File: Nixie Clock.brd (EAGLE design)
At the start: 226.4 x 128.3 mm, 136 parts, among them IC1_SECONDS_UNITS 4017N, IC2_SECONDS_TENS 4017N, IC3_MINUTES_UNITS 4017N, IC4_MINUTES_TENS 4017N, IC5_HOURS_UNITS 4017N, IC6_HOURS_TENS 4017N, T0 MPSA42, T1 MPSA42, T10 MPSA42, T11 MPSA42, T12 MPSA42, T13 MPSA42, T14 MPSA42, T15 MPSA42, T16 MPSA42, T17 MPSA42, T18 MPSA42, T19 MPSA42, T2 MPSA42, T20 MPSA42, T21 MPSA42, T22 MPSA42, T23 MPSA42, T24 MPSA42, T25 MPSA42, T26 MPSA42, T27 MPSA42, T28 MPSA42, T29 MPSA42, T3 MPSA42, T30 MPSA42, T31 MPSA42, T32 MPSA42, T33 MPSA42, T34 MPSA42, T35 MPSA42, T36 MPSA42, T37 MPSA42, T38 MPSA42, T39 MPSA42, T4 MPSA42, T40 MPSA42, T41 MPSA42, T42 MPSA42, T43 MPSA42, T44 MPSA42, T5 MPSA42, T6 MPSA42, T7 MPSA42, T8 MPSA42, T9 MPSA42

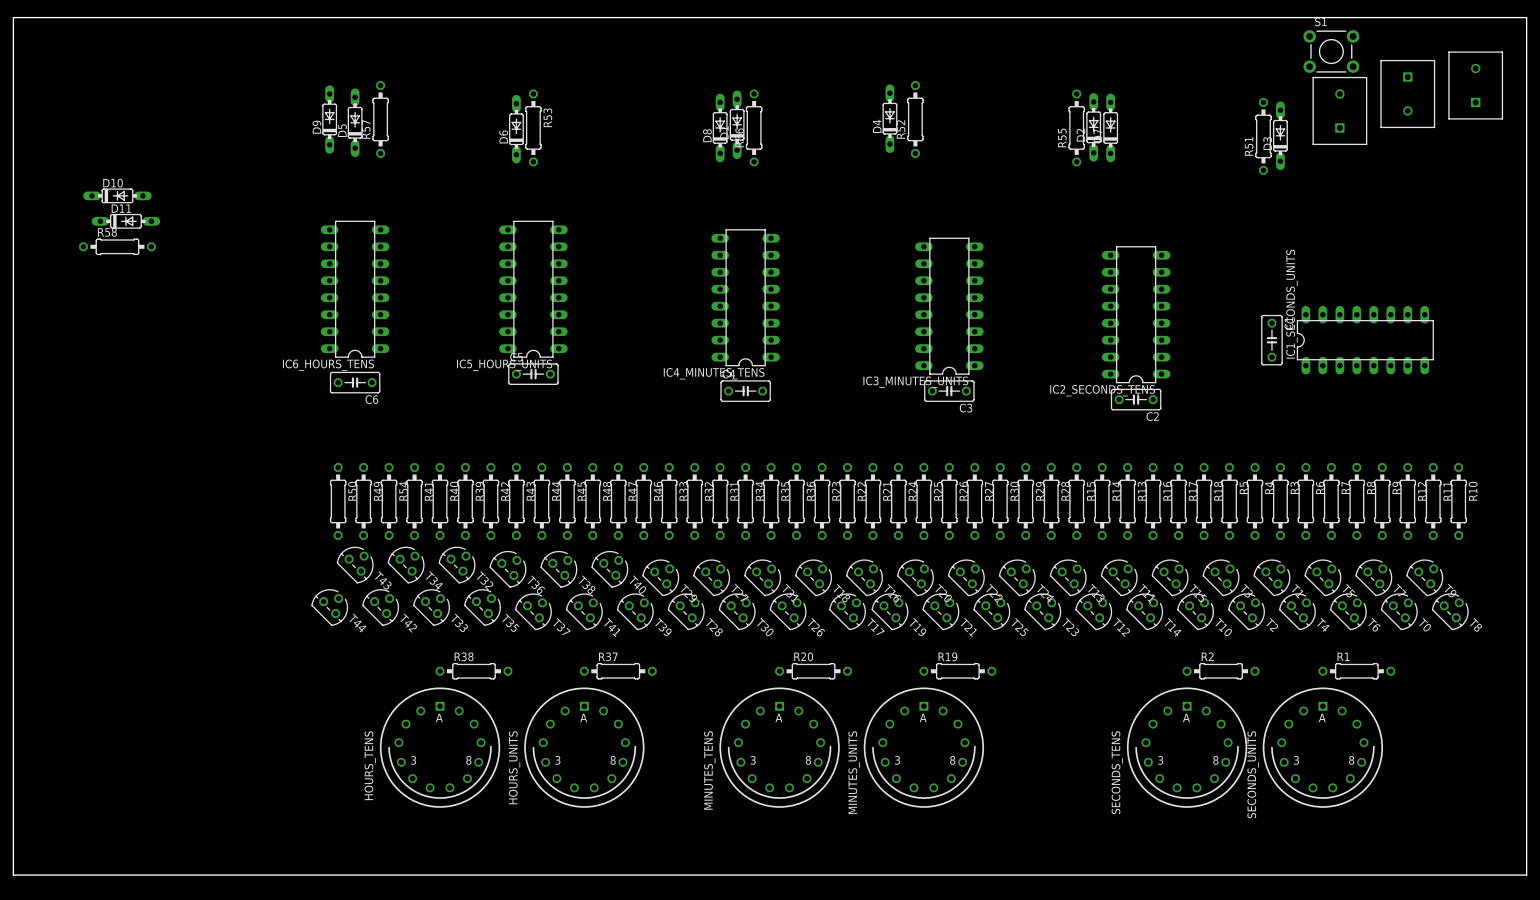
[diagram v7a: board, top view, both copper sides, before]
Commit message: Complete schematics and finish placing components
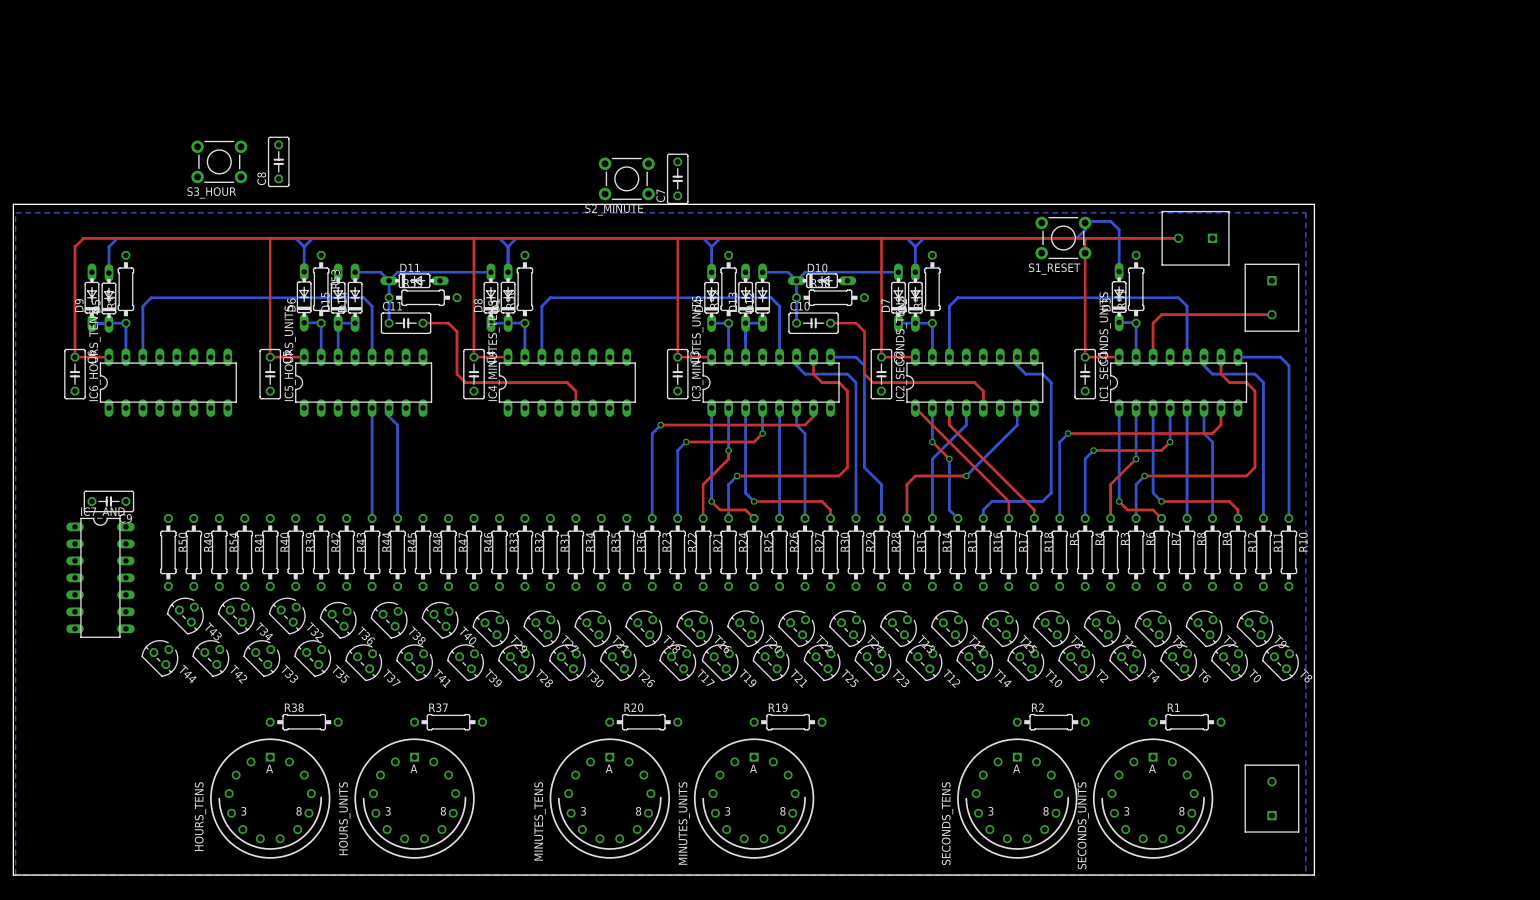
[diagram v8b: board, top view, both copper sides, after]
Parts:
- removed S1: SWITCH-MOMENTARY-2PTH, SparkFun-Electromechanical:TACTILE-PTH
- added C10, C11, C7, C8: 2.2n, resistor:C050-030X075
- added C9: 100n, resistor:C050-030X075
- added D12, D13, D14, D15: 1N4148DO35-7, diode:DO35-7
- added IC7_AND: 4081N, 40xx:DIL14
- added R59: 22k, resistor:0207/10
- added S1_RESET, S2_MINUTE, S3_HOUR: SWITCH-MOMENTARY-2PTH, SparkFun-Electromechanical:TACTILE-PTH
- R1, R19, R2, R20, R37, R38: value (none) -> 10k
- R58: value 5k -> 22k
- moved CON_HIGH_VOLTAGE 110.9 mm to (188.0, 11.4)
- moved R58 107.0 mm to (121.9, 86.4)
- moved D10 106.2 mm to (120.7, 88.9)
- moved R57 45.8 mm to (16.5, 87.6)
- moved D5 45.2 mm to (14.0, 86.2)
- moved D9 44.5 mm to (11.4, 86.4)
- moved D11 44.1 mm to (59.7, 88.9)
- moved D1 42.9 mm to (73.7, 86.4)
- moved D8 42.7 mm to (71.1, 86.4)
- moved C6 41.9 mm to (8.89, 74.9), turned to 270 degrees
- moved R56 41.9 mm to (76.2, 87.6)
- moved C4 40.7 mm to (68.6, 74.9), turned to 270 degrees
- moved C3 40.7 mm to (99.1, 74.9), turned to 270 degrees
- moved D7 40.7 mm to (132.1, 86.4)
- moved D6 40.5 mm to (43.2, 86.4)
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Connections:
- new net ADD_HOUR: C8.2, D15.A, S3_HOUR.3
- new net ADD_MINUTE: C7.2, D13.A, S2_MINUTE.3
- new net N$101: C11.2, IC4_MINUTES_TENS.5
- new net N$103: D12.C, D13.C, IC3_MINUTES_UNITS.14
- new net N$105: D14.C, D15.C, IC5_HOURS_UNITS.14
- new net N$90: C10.2, IC2_SECONDS_TENS.5
- net GND: now also C9.2, D10.A, D11.A, IC7_AND.7, R58.2, R59.2
- net HOURS_5: now also IC7_AND.1; no longer D10.C
- net INC_HOURS: now also C11.1, D11.C, D14.A, R59.1; no longer IC4_MINUTES_TENS.5, IC5_HOURS_UNITS.14
- net INC_MINUTES: now also C10.1, D10.C, D12.A, R58.1; no longer IC2_SECONDS_TENS.5, IC3_MINUTES_UNITS.14
- net MASTER_RESET: now also S1_RESET.3; no longer S1.3
- net RESET_HOURS: now also IC7_AND.3; no longer D10.A, D11.A, R58.2
- net THOURS_2: now also IC7_AND.2; no longer D11.C
- net VCC: now also C7.1, C8.1, C9.1, IC7_AND.14, S1_RESET.1, S2_MINUTE.1, S3_HOUR.1; no longer R58.1, S1.1
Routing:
- net VCC: track 0.00 -> 301.5 mm
- net MASTER_RESET: track 0.00 -> 187.1 mm
- net INC_SECONDS_TENS: track 0.00 -> 51.9 mm
- net INC_MINUTES_TENS: track 0.00 -> 51.9 mm
- net INC_HOURS_TENS: track 0.00 -> 50.6 mm
- net SEC_4: track 0.00 -> 44.0 mm, vias 0 -> 1
- net MIN_4: track 0.00 -> 44.0 mm, vias 0 -> 1
- net MIN_3: track 0.00 -> 39.2 mm, vias 0 -> 1
- net SEC_3: track 0.00 -> 39.2 mm, vias 0 -> 1
- net TSEC_4: track 0.00 -> 36.4 mm
- net N$90: track 0.00 -> 33.3 mm
- net N$101: track 0.00 -> 33.3 mm
- net MIN_9: track 0.00 -> 31.5 mm
- net SEC_9: track 0.00 -> 31.5 mm
- net SEC_8: track 0.00 -> 31.0 mm
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- added copper zone on layer 16, net GND
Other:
- board size 226.4 x 128.3 mm -> 194.6 x 100.3 mm
